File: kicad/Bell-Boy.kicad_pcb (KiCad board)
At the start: 2 copper layers, 61 x 61 mm, 18 parts

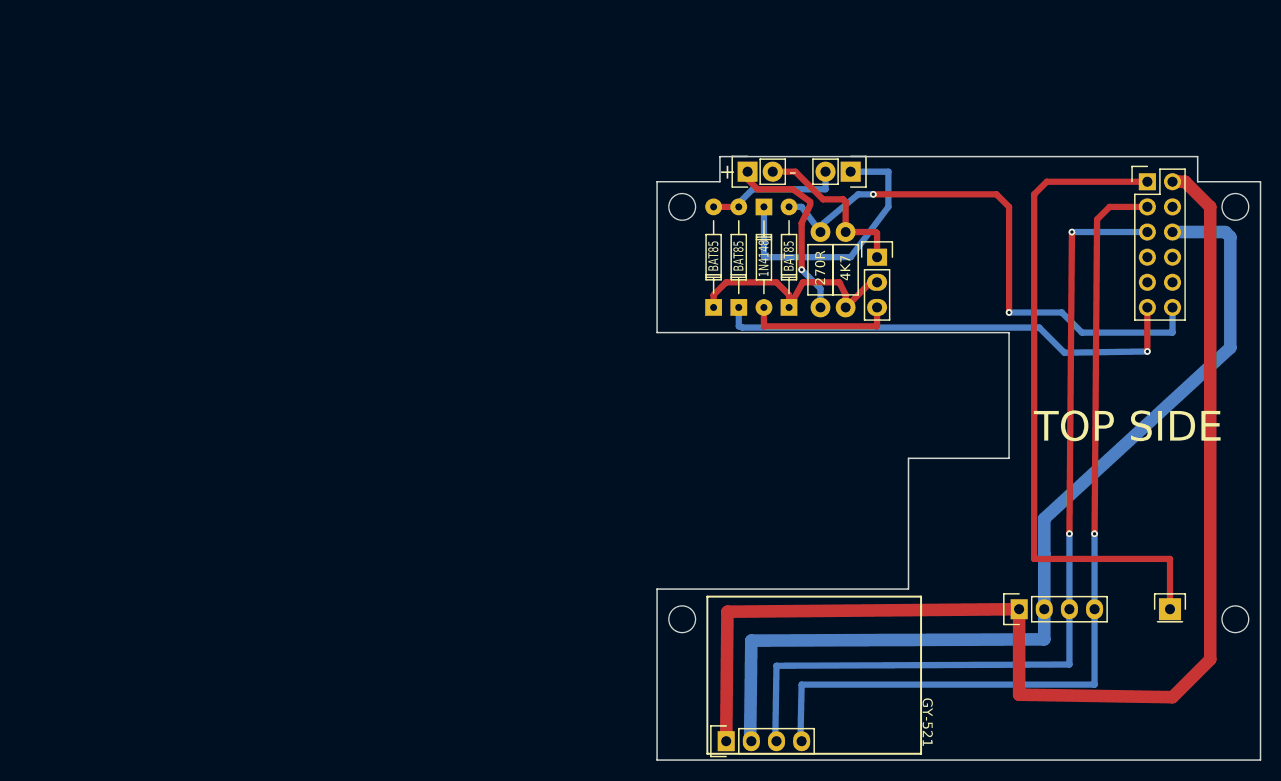
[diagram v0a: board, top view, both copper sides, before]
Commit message: Updates to new case format
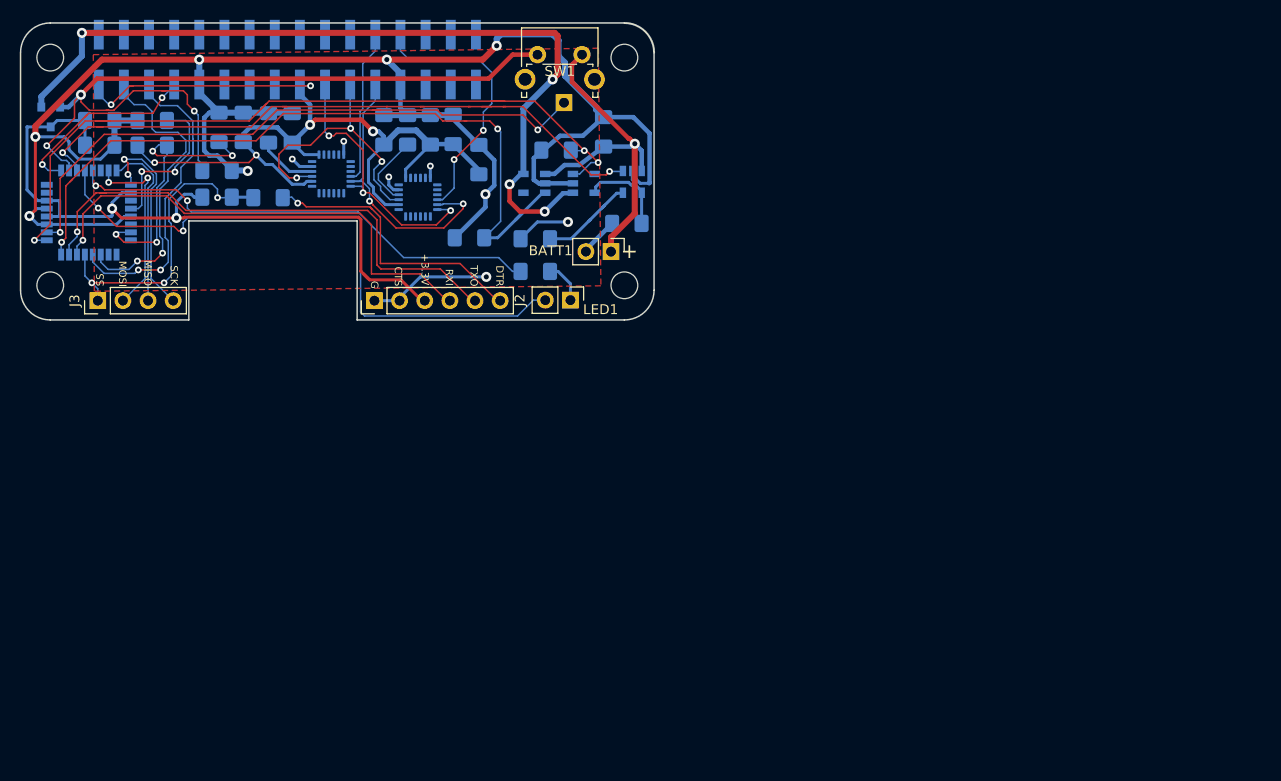
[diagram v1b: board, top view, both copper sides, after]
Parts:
- removed 1N4148, BAT85 (x3): , Diodes_ThroughHole:Diode_DO-35_SOD27_Horizontal_RM10
- removed 270R, 4K7: , Resistors_ThroughHole:Resistor_Horizontal_RM7mm
- removed the ? at (163.8, 66.0)
- removed the ? at (116.8, 110.2)
- removed the ? at (172.7, 110.2)
- removed the ? at (172.7, 68.6) (x2)
- removed the ? at (136.5, 73.7)
- removed the ? at (123.4, 65.0)
- removed the ? at (133.9, 65.0)
- removed the ? at (150.9, 109.2)
- removed the ? at (121.3, 122.6)
- removed the ? at (166.1, 109.2)
- removed the ? at (116.8, 68.6)
- added ?: , MountingHole:MountingHole_2.7mm_M2.5, F.Cu at (53.0, 53.5)
- added ?: , MountingHole:MountingHole_2.7mm_M2.5, F.Cu at (53.0, 76.5)
- added ?: , MountingHole:MountingHole_2.7mm_M2.5, F.Cu at (111.0, 53.5)
- added ?: , MountingHole:MountingHole_2.7mm_M2.5, F.Cu at (111.0, 76.5)
- added BATT1: Battery_Cell, Connector_PinHeader_2.54mm:PinHeader_1x02_P2.54mm_Vertical, F.Cu at (109.7, 73.1)
- added C1: 100n, Capacitor_SMD:C_1206_3216Metric_Pad1.42x1.75mm_HandSolder, B.Cu at (75.0, 67.7)
- added C10: 100n, Capacitor_SMD:C_1206_3216Metric_Pad1.42x1.75mm_HandSolder, B.Cu at (72.5, 60.5)
- added C11: 100n, Capacitor_SMD:C_1206_3216Metric_Pad1.42x1.75mm_HandSolder, B.Cu at (89.1, 60.8)
- added C12: 100n, Capacitor_SMD:C_1206_3216Metric_Pad1.42x1.75mm_HandSolder, B.Cu at (93.7, 60.8)
- added C13: 2.2uF, Capacitor_SMD:C_1206_3216Metric_Pad1.42x1.75mm_HandSolder, B.Cu at (96.3, 63.8)
- added C14: 2.2uf, Capacitor_SMD:C_1206_3216Metric_Pad1.42x1.75mm_HandSolder, B.Cu at (86.7, 60.8)
- added C2: 100n, Capacitor_SMD:C_1206_3216Metric_Pad1.42x1.75mm_HandSolder, B.Cu at (63.3, 59.9)
- added C3: 100n, Capacitor_SMD:C_1206_3216Metric_Pad1.42x1.75mm_HandSolder, B.Cu at (58.0, 59.9)
- added C4: 4u7, Capacitor_SMD:C_1206_3216Metric_Pad1.42x1.75mm_HandSolder, B.Cu at (58.0, 62.4)
- added C5: 4u7, Capacitor_SMD:C_1206_3216Metric_Pad1.42x1.75mm_HandSolder, B.Cu at (108.9, 61.0)
- added C6: 4u7, Capacitor_SMD:C_1206_3216Metric_Pad1.42x1.75mm_HandSolder, B.Cu at (111.2, 70.2)
- added C7: 10n, Capacitor_SMD:C_1206_3216Metric_Pad1.42x1.75mm_HandSolder, B.Cu at (77.5, 60.6)
- added C8: 10n, Capacitor_SMD:C_1206_3216Metric_Pad1.42x1.75mm_HandSolder, B.Cu at (91.4, 60.8)
- added C9: 100n, Capacitor_SMD:C_1206_3216Metric_Pad1.42x1.75mm_HandSolder, B.Cu at (75.0, 60.6)
- added D1: BAT54C, Package_TO_SOT_SMD:SOT-23, B.Cu at (53.0, 59.5)
- added J1: Conn_01x01_Male, Connector_PinHeader_2.54mm:PinHeader_1x01_P2.54mm_Vertical, B.Cu at (104.9, 58.0)
- added J2: Conn_01x06, Connector_PinHeader_2.54mm:PinHeader_1x06_P2.54mm_Vertical, F.Cu at (85.8, 78.0)
- added J3: Conn_01x04, Connector_PinHeader_2.54mm:PinHeader_1x04_P2.54mm_Vertical, F.Cu at (57.8, 78.0)
- added J4: Conn_02x16_Odd_Even, Connector_PinSocket_2.54mm:PinSocket_2x16_P2.54mm_Vertical_SMD, B.Cu at (77.0, 53.7)
- added LED1: LED_Dual_2pin, Connector_PinHeader_2.54mm:PinHeader_1x02_P2.54mm_Vertical, F.Cu at (105.5, 78.0)
- added R1: 82R, Resistor_SMD:R_1206_3216Metric_Pad1.42x1.75mm_HandSolder, B.Cu at (102.0, 75.1)
- added R2: 10K, Resistor_SMD:R_1206_3216Metric_Pad1.42x1.75mm_HandSolder, B.Cu at (95.3, 71.7)
- added R3: 4.7k, Resistor_SMD:R_1206_3216Metric_Pad1.42x1.75mm_HandSolder, B.Cu at (102.0, 71.8)
- added R4: 100k, Resistor_SMD:R_1206_3216Metric_Pad1.42x1.75mm_HandSolder, B.Cu at (70.0, 60.5)
- added R5: 10K, Resistor_SMD:R_1206_3216Metric_Pad1.42x1.75mm_HandSolder, B.Cu at (69.8, 67.6)
- added R6: 10K, Resistor_SMD:R_1206_3216Metric_Pad1.42x1.75mm_HandSolder, B.Cu at (104.1, 62.9)
- added R7: 100K, Resistor_SMD:R_1206_3216Metric_Pad1.42x1.75mm_HandSolder, B.Cu at (69.8, 64.9)
- added R8: 100k, Resistor_SMD:R_1206_3216Metric_Pad1.42x1.75mm_HandSolder, B.Cu at (63.3, 62.4)
- added SW1: SW_DIP_x01, Button_Switch_THT:SW_Tactile_SPST_Angled_PTS645Vx39-2LFS, F.Cu at (102.2, 53.2)
- added U1: ATmega328P-AU, Package_QFP:LQFP-32_7x7mm_P0.8mm, B.Cu at (56.9, 69.2)
- added U2: MAX40200, Package_TO_SOT_SMD:SOT-23-5, B.Cu at (101.9, 66.2)
- added U3: MCP73831-2-OT, Package_TO_SOT_SMD:SOT-23-5, B.Cu at (111.8, 66.0)
- added U4: MAX40200, Package_TO_SOT_SMD:SOT-23-5, B.Cu at (106.9, 66.2)
- added U5: ICM-20689, Sensor_Motion:InvenSense_QFN-24_4x4mm_P0.5mm, B.Cu at (81.4, 65.2)
- added U6: ICM-20689, Sensor_Motion:InvenSense_QFN-24_4x4mm_P0.5mm, B.Cu at (90.2, 67.6)
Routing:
- net GND: track 17.3 -> 215.8 mm, vias 0 -> 13
- net Net-(P1-Pad2): track 123.3 -> 0.00 mm
- net Net-(P1-Pad6): track 94.8 -> 0.00 mm
- net Net-(P1-Pad5): track 88.6 -> 0.00 mm, vias 2 -> 0
- net Net-(P1-Pad3): track 88.0 -> 0.00 mm, vias 1 -> 0
- net +5V: track 0.00 -> 86.2 mm, vias 0 -> 4
- net +VSW: track 0.00 -> 82.7 mm, vias 0 -> 3
- net Net-(R6-Pad1): track 0.00 -> 78.2 mm, vias 0 -> 3
- net Net-(R2-Pad1): track 0.00 -> 76.2 mm, vias 0 -> 2
- net VDDA: track 0.00 -> 74.2 mm, vias 0 -> 2
- net Net-(U1-Pad11): track 0.00 -> 67.4 mm, vias 0 -> 2
- net Net-(J1-Pad1): track 0.00 -> 63.4 mm, vias 0 -> 2
- net Net-(LED1-Pad2): track 0.00 -> 61.8 mm, vias 0 -> 2
- net Net-(D3-Pad2): track 56.4 -> 0.00 mm, vias 2 -> 0
- net Net-(J2-Pad5): track 0.00 -> 53.2 mm, vias 0 -> 1
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- added copper zone on F.Cu, net GND
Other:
- board size 61 x 61 mm -> 64 x 30 mm
- rule pad_to_mask_clearance: 0.2 -> 0.0762
- rule via_min_drill: 0.3302 -> 0.254
- rule via_min_size: 0.6858 -> 0.508
- board text added: "+3.3V"
- board text added: "CTS"
- board text added: "DTR"
- board text added: "G"
- board text added: "MISO"
- board text added: "MOSI"
- board text added: "RXI"
- board text added: "SCK"
- board text added: "SS"
- board text added: "TXO"
- board text added: "o"
- board text removed: "-"
- board text removed: "GY-521"
- board text removed: "TOP SIDE"

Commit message: Update PCB files
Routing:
- net Net-(LED1-Pad2): track 61.8 -> 58.1 mm
- net Net-(J2-Pad5): track 53.2 -> 49.5 mm
- net Net-(J2-Pad4): track 49.2 -> 46.1 mm
- net Net-(C1-Pad2): track 29.2 -> 26.3 mm
- net VDDA: track 74.2 -> 71.6 mm
- net Net-(R1-Pad2): track 48.6 -> 50.8 mm
- net Net-(C1-Pad1): track 32.4 -> 31.9 mm, vias 3 -> 2
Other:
- outline, holes or cut-outs redrawn

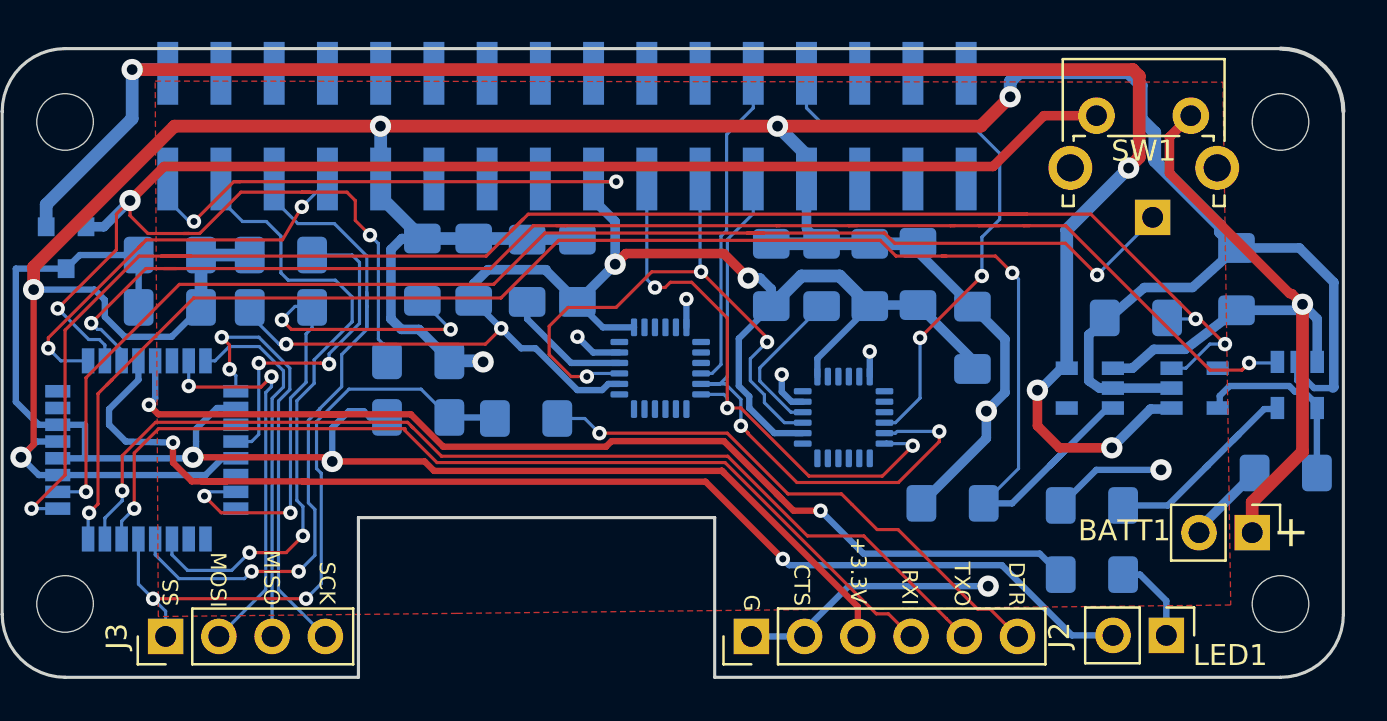
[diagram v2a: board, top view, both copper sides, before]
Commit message: Finished autotare and single IMU conversion
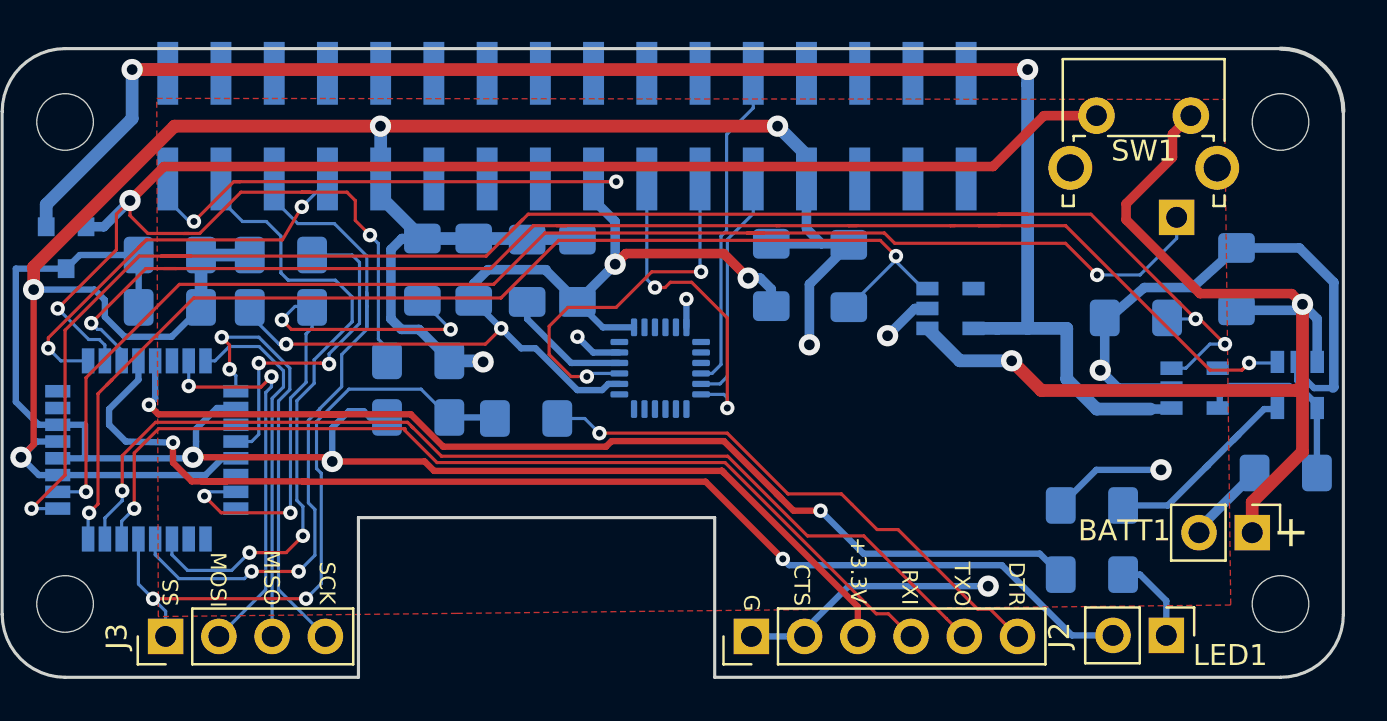
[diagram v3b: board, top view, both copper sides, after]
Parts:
- removed C11, C12: 100n, Capacitor_SMD:C_1206_3216Metric_Pad1.42x1.75mm_HandSolder
- removed C13: 2.2uF, Capacitor_SMD:C_1206_3216Metric_Pad1.42x1.75mm_HandSolder
- removed C8: 10n, Capacitor_SMD:C_1206_3216Metric_Pad1.42x1.75mm_HandSolder
- removed U6: ICM-20689, Sensor_Motion:InvenSense_QFN-24_4x4mm_P0.5mm
- C9: value 100n -> 470nF
- R4, R8: value 100k -> 10K
- moved R2 11.9 mm to (90.4, 60.9), turned to 90 degrees
- moved U2 7.66 mm to (95.2, 62.4), turned to 0 degrees
- moved J1 1.14 mm to (106.0, 58.0)
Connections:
- J4 pad 10: Net-(J4-Pad10) -> (no net)
- J4 pad 11: Net-(J4-Pad11) -> (no net)
- J4 pad 12: Net-(J4-Pad12) -> (no net)
- J4 pad 13: Net-(J4-Pad13) -> (no net)
- J4 pad 14: Net-(J4-Pad14) -> (no net)
- J4 pad 15: Net-(J4-Pad15) -> (no net)
- J4 pad 16: Net-(J4-Pad16) -> (no net)
- J4 pad 18: Net-(J4-Pad18) -> (no net)
- J4 pad 20: Net-(J4-Pad20) -> (no net)
- J4 pad 22: Net-(J4-Pad22) -> (no net)
- J4 pad 26: Net-(J4-Pad26) -> (no net)
- J4 pad 27: Net-(J4-Pad27) -> (no net)
- J4 pad 28: Net-(J4-Pad28) -> (no net)
- J4 pad 29: Net-(J4-Pad29) -> (no net)
- J4 pad 30: Net-(J4-Pad30) -> (no net)
- J4 pad 31: Net-(J4-Pad31) -> (no net)
- J4 pad 32: Net-(J4-Pad32) -> (no net)
- J4 pad 4: Net-(J4-Pad4) -> (no net)
- J4 pad 6: Net-(J4-Pad6) -> (no net)
- J4 pad 8: Net-(J4-Pad8) -> (no net)
- U1 pad 14: Net-(U1-Pad14) -> (no net)
- U1 pad 19: Net-(U1-Pad19) -> (no net)
- U1 pad 22: Net-(U1-Pad22) -> (no net)
- U1 pad 24: Net-(U1-Pad24) -> (no net)
- U1 pad 25: Net-(U1-Pad25) -> (no net)
- U1 pad 26: Net-(U1-Pad26) -> (no net)
- U1 pad 7: Net-(U1-Pad7) -> (no net)
- U1 pad 8: Net-(U1-Pad8) -> (no net)
- U2 pad 4: Net-(U2-Pad4) -> (no net)
- U4 pad 4: Net-(U4-Pad4) -> (no net)
- U5 pad 12: Net-(U5-Pad12) -> (no net)
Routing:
- net GND: track 215.8 -> 171.6 mm, vias 13 -> 12
- net Net-(J4-Pad26): track 28.2 -> 0.00 mm, vias 2 -> 0
- net +3V3: track 101.6 -> 76.1 mm
- net Net-(R2-Pad1): track 76.2 -> 54.8 mm
- net Net-(J4-Pad23): track 30.5 -> 12.4 mm, vias 2 -> 0
- net +BATT: track 37.3 -> 54.1 mm, vias 1 -> 2
- net Net-(J4-Pad19): track 29.0 -> 16.7 mm, vias 3 -> 2
- net Net-(J4-Pad21): track 30.4 -> 20.0 mm, vias 3 -> 2
- net +5V: track 86.2 -> 78.7 mm, vias 4 -> 2
- net Net-(C11-Pad1): track 7.46 -> 0.00 mm
- net Net-(J4-Pad12): track 2.00 -> 0.00 mm
- net Net-(J1-Pad1): track 63.4 -> 65.1 mm
- net Net-(J4-Pad29): track 1.00 -> 0.00 mm
- net Net-(J4-Pad22): track 1.00 -> 0.00 mm
- net Net-(J4-Pad16): track 1.00 -> 0.00 mm
